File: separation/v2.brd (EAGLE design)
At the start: 40.6 x 25.4 mm, 16 parts

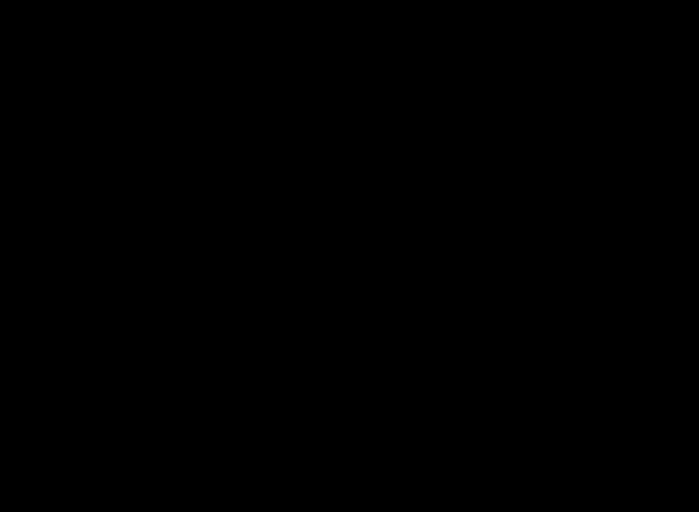
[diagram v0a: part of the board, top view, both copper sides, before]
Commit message: connect mosfet in schematic
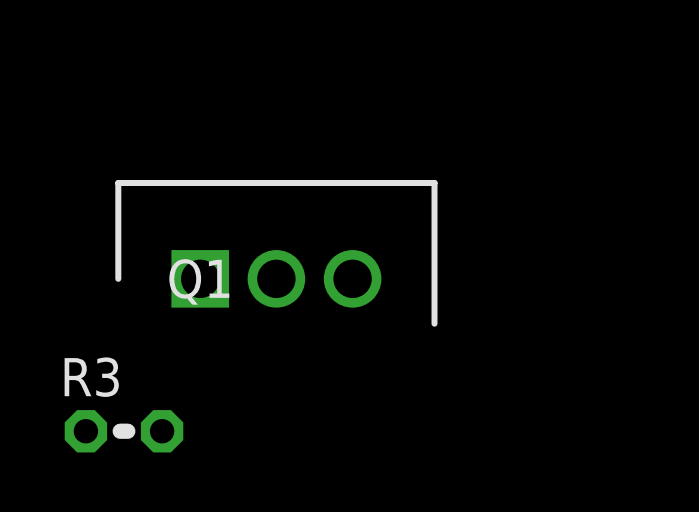
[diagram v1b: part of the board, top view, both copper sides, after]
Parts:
- added Q1: IRLZ24NPBF, SamacSys_Parts:TO254P469X1042X1967-3P
- added R3: (no value), rcl:0204V
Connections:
- removed net A3: MCU-L.4
- new net SER-: Q1.3, SERCON.1
- new net SERPOW: MCU-L.4, Q1.1, R3.1
- net GND: now also Q1.2, R3.2; no longer SERCON.1
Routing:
- net SERPOW: track 0.00 -> 1.80 mm
- net A3: track 1.80 -> 0.00 mm
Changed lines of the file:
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@@
 <attribute name="VALUE" x="-16.274053125" y="20.691978125" size="0.635" layer="21" font="vector" ratio="10"/>
+</element>
+<element name="Q1" library="SamacSys_Parts" package="TO254P469X1042X1967-3P" value="IRLZ24NPBF" x="-20.32" y="-12.7" smashed="yes">
+<attribute name="ALLIED_NUMBER" value="70017119" x="-20.32" y="-12.7" size="1.778" layer="27" display="off"/>
+<attribute name="DESCRIPTION" value="MOSFET MOSFT 55V 18A 60mOhm 10nC LogLvlAB" x="-20.32" y="-12.7" size="1.778" layer="27" display="off"/>
+<attribute name="HEIGHT" value="4.69mm" x="-20.32" y="-12.7" size="1.778" layer="27" display="off"/>
+<attribute name="MANUFACTURER_NAME" value="Infineon" x="-20.32" y="-12.7" size="1.778" layer="27" display="off"/>
+<attribute name="MANUFACTURER_PART_NUMBER" value="IRLZ24NPBF" x="-20.32" y="-12.7" size="1.778" layer="27" display="off"/>
+<attribute name="NAME" x="-20.32" y="-12.7" size="1.27" layer="25" align="center"/>
+<attribute name="RS_PART_NUMBER" value="5411231P" x="-20.32" y="-12.7" size="1.778" layer="27" display="off"/>
+<attribute name="RS_PRICE-STOCK" value="http://uk.rs-online.com/web/p/products/5411231P" x="-20.32" y="-12.7" size="1.778" layer="27" display="off"/>
+<attribute name="VALUE" x="-20.32" y="-12.7" size="1.27" layer="27" align="center"/>
+</element>
+<element name="R3" library="rcl" library_urn="urn:adsk.eagle:library:334" package="0204V" package3d_urn="urn:adsk.eagle:package:23495/1" value="" x="-22.86" y="-17.78" smashed="yes">
+<attribute name="NAME" x="-24.9936" y="-16.6116" size="1.27" layer="25" ratio="10"/>
+<attribute name="POPULARITY" value="11" x="-22.86" y="-17.78" size="1.778" layer="27" display="off"/>
+<attribute name="SPICEPREFIX" value="R" x="-22.86" y="-17.78" size="1.778" layer="27" display="off"/>
+<attribute name="VALUE" x="-24.9936" y="-20.0914" size="1.27" layer="27" ratio="10"/>
 </element>
 </elements>
@@
 <contactref element="LOUD" pad="2"/>
 <contactref element="R2" pad="2"/>
-<contactref element="SERCON" pad="1"/>
 <wire x1="7.62" y1="17.9705" x2="9.3345" y2="17.9705" width="1.524" layer="1"/>
 <wire x1="9.3345" y1="17.9705" x2="9.398" y2="17.907" width="1.524" layer="1"/>
@@
 <contactref element="C1" pad="1"/>
 <contactref element="C2" pad="1"/>
+<contactref element="Q1" pad="2"/>
+<contactref element="R3" pad="2"/>
+<wire x1="-17.78" y1="-12.7" x2="-21.59" y2="-17.78" width="0" layer="19" extent="1-1"/>
+<wire x1="-15.113" y1="12.136" x2="-17.78" y2="-12.7" width="0" layer="19" extent="1-1"/>
+<wire x1="-14.859" y1="16.891" x2="-15.113" y2="12.136" width="0" layer="19" extent="1-1"/>
+<wire x1="-12.192" y1="16.891" x2="-14.859" y2="16.891" width="0" layer="19" extent="1-1"/>
+<wire x1="7.62" y1="17.9705" x2="-12.192" y2="16.891" width="0" layer="19" extent="1-1"/>
+<wire x1="14.224" y1="17.155" x2="9.398" y2="17.907" width="0" layer="19" extent="1-1"/>
+<wire x1="17.335" y1="6.35" x2="17.653" y2="17.399" width="0" layer="19" extent="1-1"/>
+<wire x1="9.915025" y1="3.184025" x2="17.335" y2="6.35" width="0" layer="19" extent="1-1"/>
 </signal>
 <signal name="MOSI">
@@
 <wire x1="7.62" y1="7.8105" x2="9.3345" y2="7.8105" width="1.524" layer="1"/>
 <wire x1="9.3345" y1="7.8105" x2="9.398" y2="7.747" width="1.524" layer="1"/>
-</signal>
-<signal name="A3">
-<contactref element="MCU-L" pad="4"/>
-<wire x1="-7.62" y1="12.8905" x2="-9.3345" y2="12.8905" width="1.524" layer="1"/>
-<wire x1="-9.3345" y1="12.8905" x2="-9.398" y2="12.827" width="1.524" layer="1"/>
 </signal>
 <signal name="SDA">
@@
 <wire x1="-9.3345" y1="20.5105" x2="-9.398" y2="20.574" width="1.524" layer="1"/>
 </signal>
+<signal name="SER-" class="1">
+<contactref element="SERCON" pad="1"/>
+<contactref element="Q1" pad="3"/>
+<wire x1="-17.526" y1="3.556" x2="-15.24" y2="-12.7" width="0" layer="19" extent="1-1"/>
+</signal>
+<signal name="SERPOW">
+<contactref element="Q1" pad="1"/>
+<contactref element="MCU-L" pad="4"/>
+<wire x1="-7.62" y1="12.8905" x2="-9.3345" y2="12.8905" width="1.524" layer="1"/>
+<wire x1="-9.3345" y1="12.8905" x2="-9.398" y2="12.827" width="1.524" layer="1"/>
+<contactref element="R3" pad="1"/>
+<wire x1="-20.32" y1="-12.7" x2="-24.13" y2="-17.78" width="0" layer="19" extent="1-1"/>
+<wire x1="-9.398" y1="12.827" x2="-20.32" y2="-12.7" width="0" layer="19" extent="1-1"/>
+</signal>
 </signals>

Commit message: remake outline
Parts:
- moved R3 18.9 mm to (-15.9, -0.25)
- moved Q1 15.9 mm to (-17.1, 2.92)
- moved R1 8.87 mm to (-0.13, 0.25), turned to 0 degrees
- moved SERCON 8.18 mm to (-7.62, 0.00)
- moved R2 4.21 mm to (5.33, 0.25), turned to 0 degrees
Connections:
- net GND: now also Q1.3; no longer Q1.2
- net SER-: now also Q1.2; no longer Q1.3
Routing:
- net SERPOW: track 1.80 -> 28.5 mm
- net SERVO: track 15.9 -> 1.78 mm
- net VSENSE: track 47.8 -> 35.4 mm
- net SER-: track 0.00 -> 5.95 mm
- net VBAT: track 5.13 -> 0.13 mm
- removed copper zone on layer 16, net GND
- removed copper zone on layer 1, net VBAT
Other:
- board size 40.6 x 25.4 mm -> 40.6 x 27.9 mm
- board text added: "COM"
- board text added: "CON/SER-/GND"
- board text added: "GATE/DRAIN/SOURCE"
- board text added: "SER-"
- board text removed: "SERVO"

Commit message: remake pours
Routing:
- added copper zone on layer 16, net GND
- added copper zone on layer 1, net VBAT
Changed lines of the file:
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@@
 <contactref element="Q1" pad="3"/>
 <contactref element="R3" pad="2"/>
-<wire x1="9.398" y1="17.907" x2="14.224" y2="17.155" width="0" layer="19" extent="1-1"/>
-<wire x1="17.335" y1="6.35" x2="17.653" y2="17.399" width="0" layer="19" extent="1-1"/>
-<wire x1="6.604" y1="0.254" x2="17.335" y2="6.35" width="0" layer="19" extent="1-1"/>
-<wire x1="-12.065" y1="2.921" x2="6.604" y2="0.254" width="0" layer="19" extent="1-1"/>
-<wire x1="-14.605" y1="-0.254" x2="-12.065" y2="2.921" width="0" layer="19" extent="1-1"/>
-<wire x1="-15.113" y1="12.136" x2="-12.065" y2="2.921" width="0" layer="19" extent="1-1"/>
-<wire x1="-14.859" y1="16.891" x2="-15.113" y2="12.136" width="0" layer="19" extent="1-1"/>
-<wire x1="-12.192" y1="16.891" x2="-14.859" y2="16.891" width="0" layer="19" extent="1-1"/>
+<polygon width="0.508" layer="16">
+<vertex x="-25.4" y="25.4"/>
+<vertex x="-20.32" y="30.48"/>
+<vertex x="19.05" y="30.48"/>
+<vertex x="25.4" y="24.13"/>
+<vertex x="25.4" y="-1.27"/>
+<vertex x="25.4" y="-3.81"/>
+<vertex x="21.59" y="-7.62"/>
+<vertex x="-20.32" y="-7.62"/>
+<vertex x="-21.59" y="-7.62"/>
+<vertex x="-26.67" y="-2.54"/>
+<vertex x="-26.67" y="24.13"/>
+</polygon>
 </signal>
 <signal name="MOSI">
@@
 <contactref element="C2" pad="2"/>
 <wire x1="-1.397" y1="0.254" x2="-1.524" y2="0.254" width="1.016" layer="1"/>
-<wire x1="-1.397" y1="0.254" x2="14.224" y2="14.605" width="0" layer="19" extent="1-1"/>
-<wire x1="-7.62" y1="0" x2="-1.524" y2="0.254" width="0" layer="19" extent="1-1"/>
-<wire x1="-15.113" y1="8.636" x2="-7.62" y2="0" width="0" layer="19" extent="1-1"/>
-<wire x1="-14.859" y1="19.431" x2="-15.113" y2="8.636" width="0" layer="19" extent="1-1"/>
+<polygon width="0.508" layer="1">
+<vertex x="-20.32" y="27.94"/>
+<vertex x="-22.86" y="25.4"/>
+<vertex x="-22.86" y="-1.27"/>
+<vertex x="-22.86" y="-2.54"/>
+<vertex x="-20.32" y="-5.08"/>
+<vertex x="19.05" y="-5.08"/>
+<vertex x="22.86" y="-1.27"/>
+<vertex x="22.86" y="22.86"/>
+<vertex x="17.78" y="27.94"/>
+<vertex x="12.7" y="27.94"/>
+</polygon>
 </signal>
 <signal name="SERVO">
@@
 <contactref element="MCU-L" pad="3"/>
 <wire x1="-7.62" y1="15.4305" x2="-9.398" y2="15.4305" width="1.524" layer="1"/>
-<wire x1="-9.398" y1="15.4305" x2="-5.08" y2="0" width="0" layer="19" extent="1-1"/>
+<wire x1="-5.08" y1="0" x2="-7.62" y2="15.4305" width="0" layer="19" extent="1-1"/>
 </signal>
 <signal name="BUZZ">

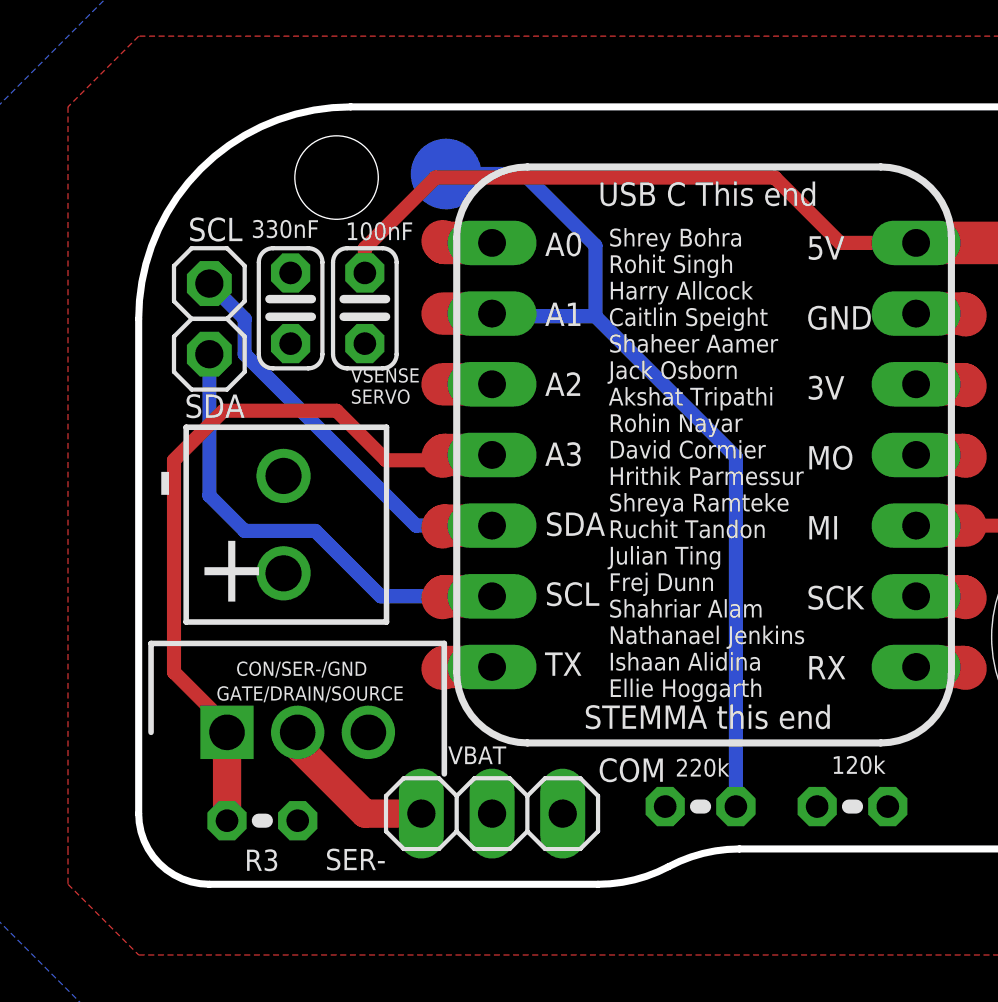
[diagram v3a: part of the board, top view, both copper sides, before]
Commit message: complete mosfet integration
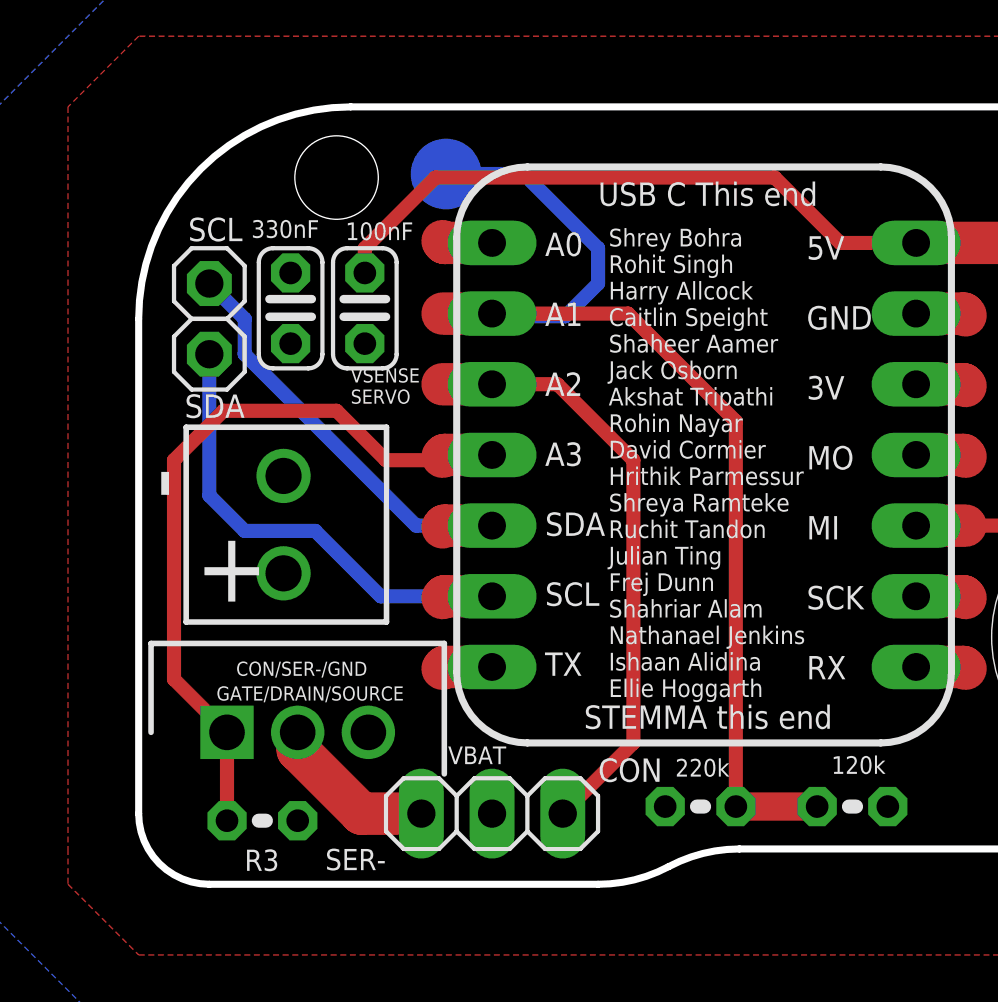
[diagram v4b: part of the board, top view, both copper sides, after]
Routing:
- net SERVO: track 1.78 -> 21.7 mm
- net VSENSE: track 35.4 -> 42.3 mm
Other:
- board text added: "CON"
- board text removed: "COM"
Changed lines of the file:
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@@
 <layer number="27" name="tValues" color="7" fill="1" visible="yes" active="yes"/>
 <layer number="28" name="bValues" color="7" fill="1" visible="yes" active="yes"/>
-<layer number="29" name="tStop" color="7" fill="3" visible="yes" active="yes"/>
+<layer number="29" name="tStop" color="7" fill="3" visible="no" active="yes"/>
 <layer number="30" name="bStop" color="7" fill="6" visible="yes" active="yes"/>
 <layer number="31" name="tCream" color="7" fill="4" visible="no" active="yes"/>
-<layer number="32" name="bCream" color="7" fill="5" visible="yes" active="yes"/>
+<layer number="32" name="bCream" color="7" fill="5" visible="no" active="yes"/>
 <layer number="33" name="tFinish" color="6" fill="3" visible="no" active="yes"/>
 <layer number="34" name="bFinish" color="6" fill="6" visible="no" active="yes"/>
@@
 <layer number="36" name="bGlue" color="7" fill="5" visible="no" active="yes"/>
 <layer number="37" name="tTest" color="7" fill="1" visible="no" active="yes"/>
-<layer number="38" name="bTest" color="7" fill="1" visible="yes" active="yes"/>
+<layer number="38" name="bTest" color="7" fill="1" visible="no" active="yes"/>
 <layer number="39" name="tKeepout" color="4" fill="11" visible="no" active="yes"/>
 <layer number="40" name="bKeepout" color="1" fill="11" visible="no" active="yes"/>
@@
 <layer number="42" name="bRestrict" color="1" fill="10" visible="no" active="yes"/>
 <layer number="43" name="vRestrict" color="2" fill="10" visible="no" active="yes"/>
-<layer number="44" name="Drills" color="7" fill="1" visible="yes" active="yes"/>
-<layer number="45" name="Holes" color="7" fill="1" visible="yes" active="yes"/>
+<layer number="44" name="Drills" color="7" fill="1" visible="no" active="yes"/>
+<layer number="45" name="Holes" color="7" fill="1" visible="no" active="yes"/>
 <layer number="46" name="Milling" color="3" fill="1" visible="no" active="yes"/>
 <layer number="47" name="Measures" color="7" fill="1" visible="yes" active="yes"/>
@@
 <layer number="49" name="Reference" color="7" fill="1" visible="yes" active="yes"/>
 <layer number="50" name="dxf" color="7" fill="1" visible="no" active="no"/>
-<layer number="51" name="tDocu" color="6" fill="1" visible="yes" active="yes"/>
+<layer number="51" name="tDocu" color="6" fill="1" visible="no" active="yes"/>
 <layer number="52" name="bDocu" color="7" fill="1" visible="no" active="yes"/>
 <layer number="53" name="tGND_GNDA" color="7" fill="9" visible="no" active="no"/>
@@
 <text x="-11.43" y="-1.27" size="0.762" layer="21" font="vector" ratio="12" rot="R180">SER-</text>
 <text x="-7.112" y="2.413" size="0.635" layer="21" font="vector" rot="R180">VBAT</text>
-<text x="-3.81" y="1.143" size="0.8382" layer="21" font="vector">COM</text>
+<text x="-3.81" y="1.143" size="0.8382" layer="21" font="vector">CON</text>
 <text x="-18.288" y="7.62" size="2.54" layer="21" font="vector">+</text>
 <text x="-18.415" y="11.303" size="2.54" layer="21" font="vector" rot="R90">-</text>
@@
 <contactref element="MCU-L" pad="3"/>
 <wire x1="-7.62" y1="15.4305" x2="-9.398" y2="15.4305" width="1.524" layer="1"/>
-<wire x1="-5.08" y1="0" x2="-7.62" y2="15.4305" width="0" layer="19" extent="1-1"/>
+<wire x1="-5.08" y1="0" x2="-2.54" y2="2.54" width="0.508" layer="1"/>
+<wire x1="-2.54" y1="2.54" x2="-2.54" y2="12.7" width="0.508" layer="1"/>
+<wire x1="-2.54" y1="12.7" x2="-5.2705" y2="15.4305" width="0.508" layer="1"/>
+<wire x1="-5.2705" y1="15.4305" x2="-7.62" y2="15.4305" width="0.508" layer="1"/>
 </signal>
 <signal name="BUZZ">
@@
 <wire x1="-7.4295" y1="17.78" x2="-7.52475" y2="17.87525" width="0.254" layer="16"/>
 <wire x1="-7.52475" y1="17.87525" x2="-7.62" y2="17.9705" width="0.254" layer="16"/>
-<wire x1="1.143" y1="0.254" x2="1.143" y2="12.827" width="0.508" layer="16"/>
-<wire x1="-3.90525" y1="17.87525" x2="-7.52475" y2="17.87525" width="0.508" layer="16"/>
-<wire x1="1.143" y1="12.827" x2="-3.90525" y2="17.87525" width="0.508" layer="16"/>
-<wire x1="-3.90525" y1="20.41525" x2="-3.90525" y2="17.87525" width="0.508" layer="16"/>
-<wire x1="-6.477" y1="22.987" x2="-3.90525" y2="20.41525" width="0.508" layer="16"/>
-<wire x1="1.143" y1="0.254" x2="4.064" y2="0.254" width="0" layer="19" extent="1-1"/>
+<wire x1="1.143" y1="0.254" x2="4.064" y2="0.254" width="1.016" layer="1"/>
+<wire x1="-3.81" y1="20.32" x2="-3.81" y2="19.05" width="0.508" layer="16"/>
+<wire x1="-3.81" y1="19.05" x2="-4.98475" y2="17.87525" width="0.508" layer="16"/>
+<wire x1="-4.98475" y1="17.87525" x2="-7.52475" y2="17.87525" width="0.508" layer="16"/>
+<wire x1="-6.477" y1="22.987" x2="-3.81" y2="20.32" width="0.508" layer="16"/>
+<wire x1="-7.62" y1="17.9705" x2="-2.7305" y2="17.9705" width="0.508" layer="1"/>
+<wire x1="1.143" y1="14.097" x2="1.143" y2="0.254" width="0.508" layer="1"/>
+<wire x1="-2.7305" y1="17.9705" x2="1.143" y2="14.097" width="0.508" layer="1"/>
 </signal>
 <signal name="A0">
@@
 <contactref element="SERCON" pad="1"/>
 <contactref element="Q1" pad="2"/>
-<wire x1="-10.16" y1="0" x2="-12.192" y2="0" width="1.016" layer="1"/>
-<wire x1="-12.192" y1="0" x2="-14.605" y2="2.413" width="1.016" layer="1"/>
-<wire x1="-14.605" y1="2.413" x2="-14.605" y2="2.921" width="1.016" layer="1"/>
+<wire x1="-14.605" y1="2.921" x2="-14.605" y2="2.286" width="1.524" layer="1"/>
+<wire x1="-14.605" y1="2.286" x2="-12.319" y2="0" width="1.524" layer="1"/>
+<wire x1="-12.319" y1="0" x2="-10.16" y2="0" width="1.524" layer="1"/>
 </signal>
 <signal name="SERPOW">
@@
 <wire x1="-11.43" y1="12.7" x2="-7.8105" y2="12.7" width="0.508" layer="1"/>
 <wire x1="-7.8105" y1="12.7" x2="-7.62" y2="12.8905" width="0.508" layer="1"/>
-<wire x1="-17.145" y1="3.175" x2="-19.05" y2="5.08" width="0.508" layer="1"/>
-<wire x1="-19.05" y1="5.08" x2="-19.05" y2="12.7" width="0.508" layer="1"/>
-<wire x1="-19.05" y1="12.7" x2="-17.272" y2="14.478" width="0.508" layer="1"/>
+<wire x1="-17.272" y1="14.478" x2="-19.05" y2="12.7" width="0.508" layer="1"/>
 <contactref element="Q1" pad="1"/>
 <contactref element="R3" pad="1"/>
-<wire x1="-17.145" y1="-0.254" x2="-17.145" y2="3.175" width="1.016" layer="1"/>
-<wire x1="-17.145" y1="-0.254" x2="-17.145" y2="2.921" width="0" layer="19" extent="1-1"/>
+<wire x1="-19.05" y1="4.826" x2="-17.145" y2="2.921" width="0.508" layer="1"/>
+<wire x1="-19.05" y1="12.7" x2="-19.05" y2="4.826" width="0.508" layer="1"/>
+<wire x1="-17.145" y1="2.921" x2="-17.145" y2="-0.254" width="0.508" layer="1"/>
 </signal>
 </signals>
